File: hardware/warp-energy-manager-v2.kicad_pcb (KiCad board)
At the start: 4 copper layers, 68 x 87 mm, 118 parts, among them J101 Boot, J102 DM3CS, P101 CON-SENSOR2, P102 SG-Ready, P103 L+N, P104 OUT, P105 INPUT, P110 MODBUS, P111 Debug, Q101 2N7002P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

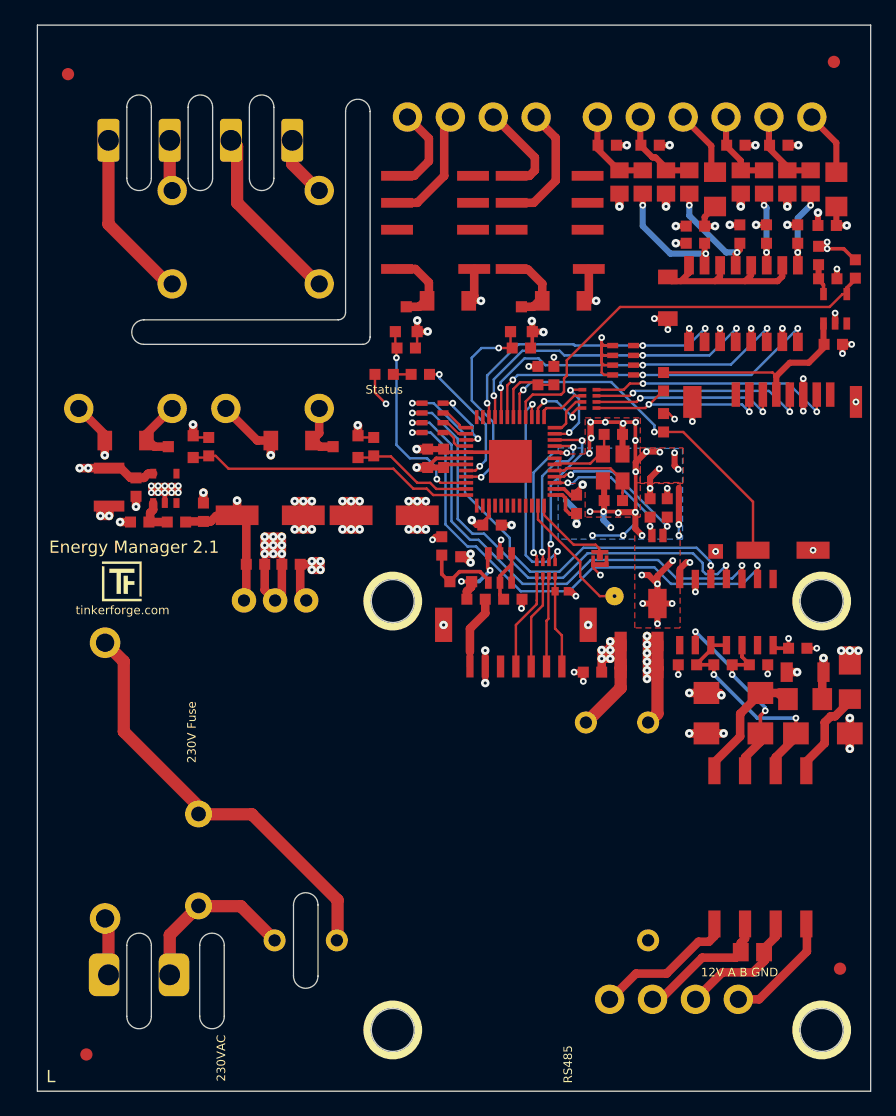
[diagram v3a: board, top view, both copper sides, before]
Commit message: hardware version 2.2 : changed connector overhang by +1,5mm
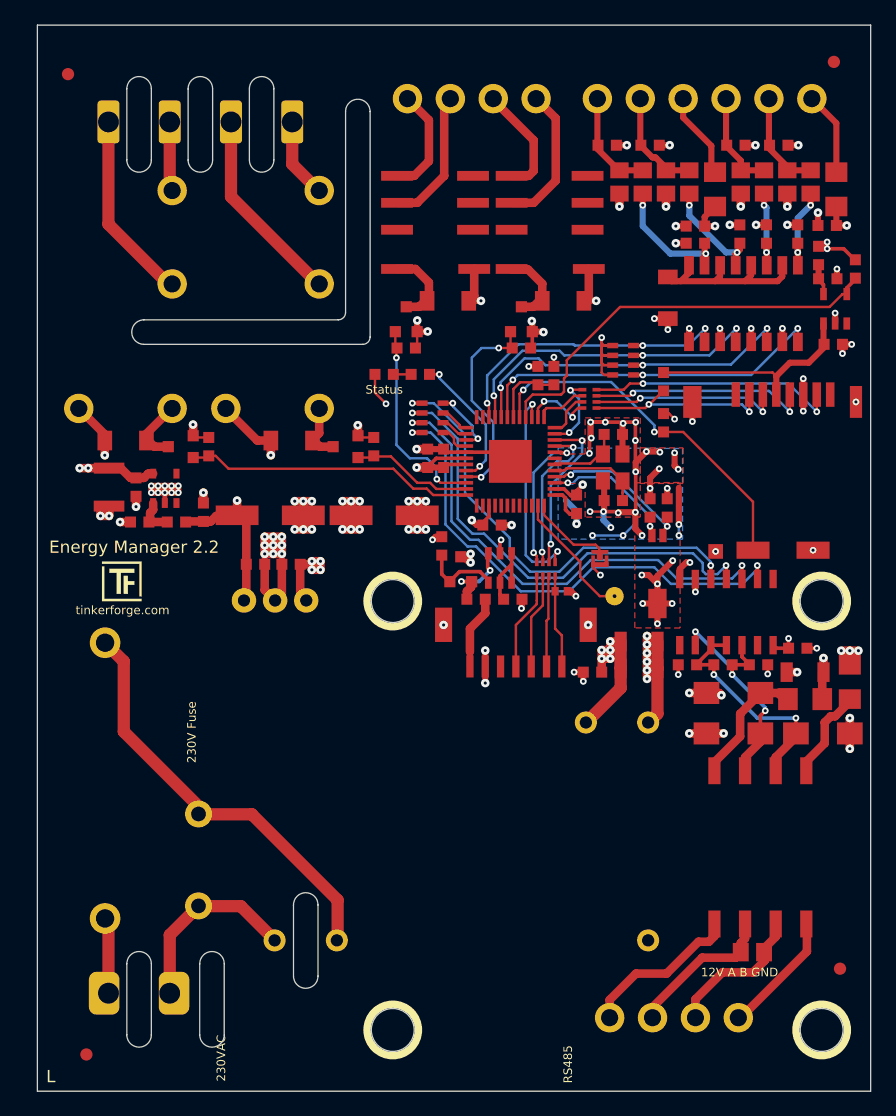
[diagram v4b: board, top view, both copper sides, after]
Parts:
- moved P102 1.50 mm to (127.8, 57.5)
- moved P103 1.50 mm to (100.7, 130.6)
- moved P104 1.50 mm to (105.7, 59.5)
- moved P105 1.50 mm to (146.8, 57.5)
- moved P110 1.50 mm to (144.3, 132.6)
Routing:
- net Net-(P102-P1): track 10.1 -> 11.7 mm
- net Net-(P105-P1): track 5.30 -> 6.83 mm
- net Net-(P102-P3): track 9.77 -> 11.3 mm
- net Net-(P110-P3): track 10.2 -> 11.7 mm
- net Net-(P105-P6): track 7.00 -> 8.50 mm
- net Net-(P105-P5): track 7.29 -> 8.79 mm
- net Net-(P104-P4): track 14.1 -> 15.6 mm
- net Net-(P104-P3): track 4.23 -> 5.73 mm
- net Net-(P104-P1): track 5.06 -> 6.56 mm
- net Net-(P103-P1): track 4.72 -> 6.22 mm
- net Net-(P102-P4): track 7.62 -> 9.12 mm
- net N: track 14.0 -> 15.5 mm
- net Net-(P105-P3): track 6.72 -> 8.22 mm
- net Net-(P105-P2): track 6.84 -> 8.34 mm
- net Net-(P104-P2): track 14.8 -> 16.3 mm
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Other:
- outline, holes or cut-outs redrawn
- board text added: "Energy Manager 2.2"
- board text removed: "Energy Manager 2.1"

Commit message: change varistor value
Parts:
- R128: value MOV-10D391KTR -> MOV-10D431KTR
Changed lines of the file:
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@@
 			)
 		)
-		(property "Value" "MOV-10D391KTR"
+		(property "Value" "MOV-10D431KTR"
 			(at 0.05 0.2 90)
 			(layer "F.Fab")

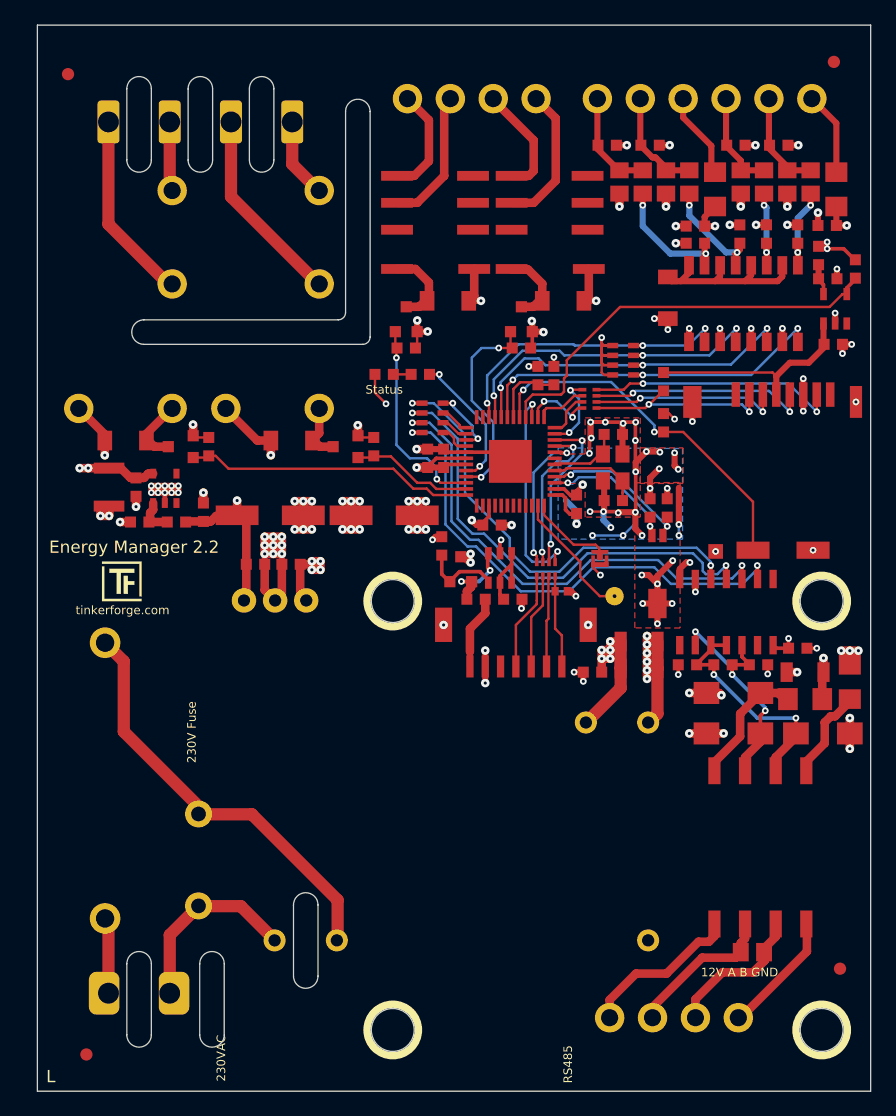
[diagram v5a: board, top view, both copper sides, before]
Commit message: add logos
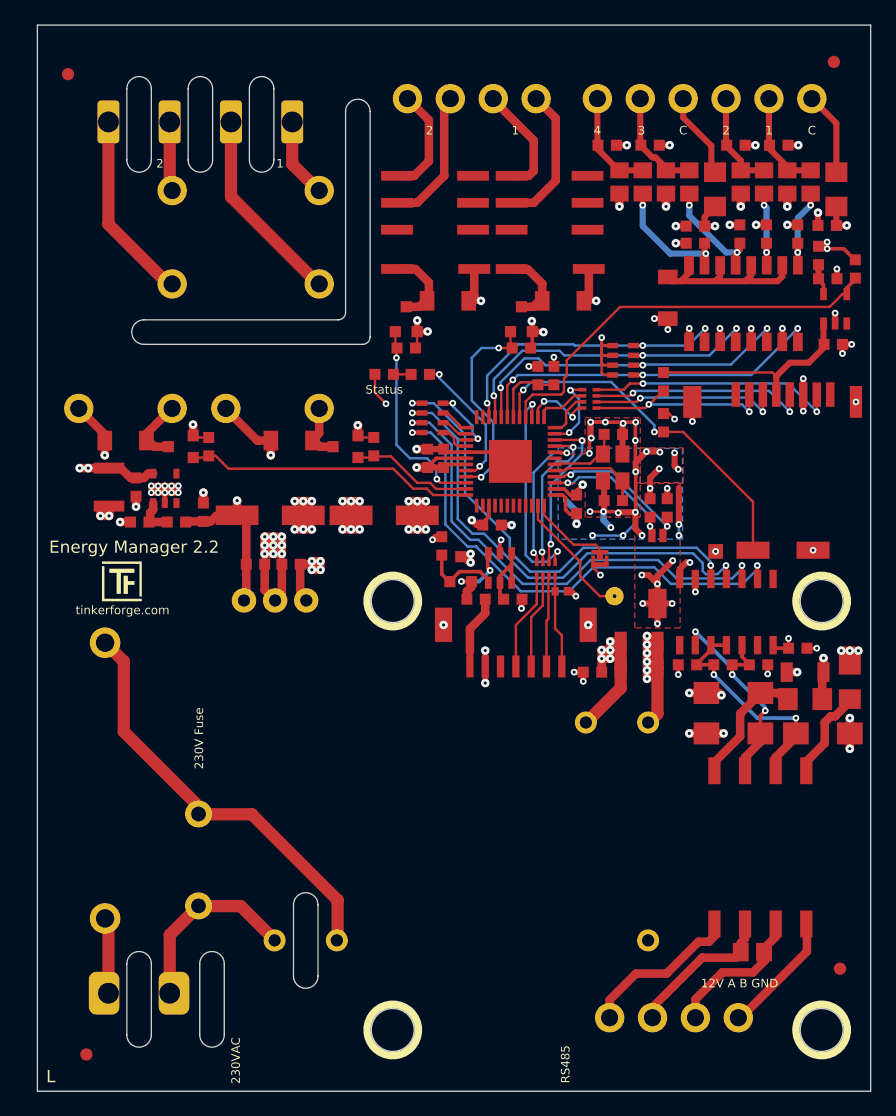
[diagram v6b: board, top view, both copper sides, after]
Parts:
- added G***: LOGO, tf:LogoWARP_15x3, B.Cu at (126.3, 109.5)
- added VAL: WEEE_7mm, tf:WEEE_7mm, B.Cu at (126.3, 123.5)
- added VAL: CE_5mm, kicad-libraries:CE_5mm, B.Cu at (126.3, 115.5)
- R104, R105, R115, R116: value 2k2 -> 4k7
- R111, R119: value 1k -> 2k2
- R112, R117, R120, R121: value 680 -> 1k
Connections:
- Q101 pad G: SG-OUT-1 -> SG-OUT-0
- Q102 pad G: RELAY1 -> RELAY0
- Q103 pad G: SG-OUT-0 -> SG-OUT-1
- Q107 pad G: RELAY0 -> RELAY1
- R102 pad 2: SG-OUT-1 -> SG-OUT-0
- R110 pad 2: RELAY1 -> RELAY0
- R113 pad 2: RELAY0 -> RELAY1
- R118 pad 2: SG-OUT-0 -> SG-OUT-1
- U101 pad 21: SG-OUT-1 -> SG-OUT-0
- U101 pad 22: SG-OUT-0 -> SG-OUT-1
- U101 pad 23: RELAY1 -> RELAY0
- U101 pad 24: RELAY0 -> RELAY1
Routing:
- net RELAY1: track 10.1 -> 23.7 mm
- net RELAY0: track 23.7 -> 10.1 mm
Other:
- board text added: "1"
- board text added: "2"
- board text added: "2 1"
- board text added: "3"
- board text added: "4"
- board text added: "4 3 C 2 1 C"
- board text added: "C"
- board text added: "Eingänge"
- board text added: "SG-Ready"
- board text removed: "Input A IN1 IN2 COM Input B IN1 IN2 COM"
- board text removed: "Relais COMA NOA COMB NOB"
- board text removed: "SG-Ready COM1 NO1 COM2 NO2"
